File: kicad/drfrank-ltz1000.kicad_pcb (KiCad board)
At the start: 2 copper layers, 79.9 x 49.9 mm, 58 parts, among them IC1 LT1013, IC2 LTZ1000A, IC3 MAX420, J10 LINK, J11 LINK, Q1 BC639

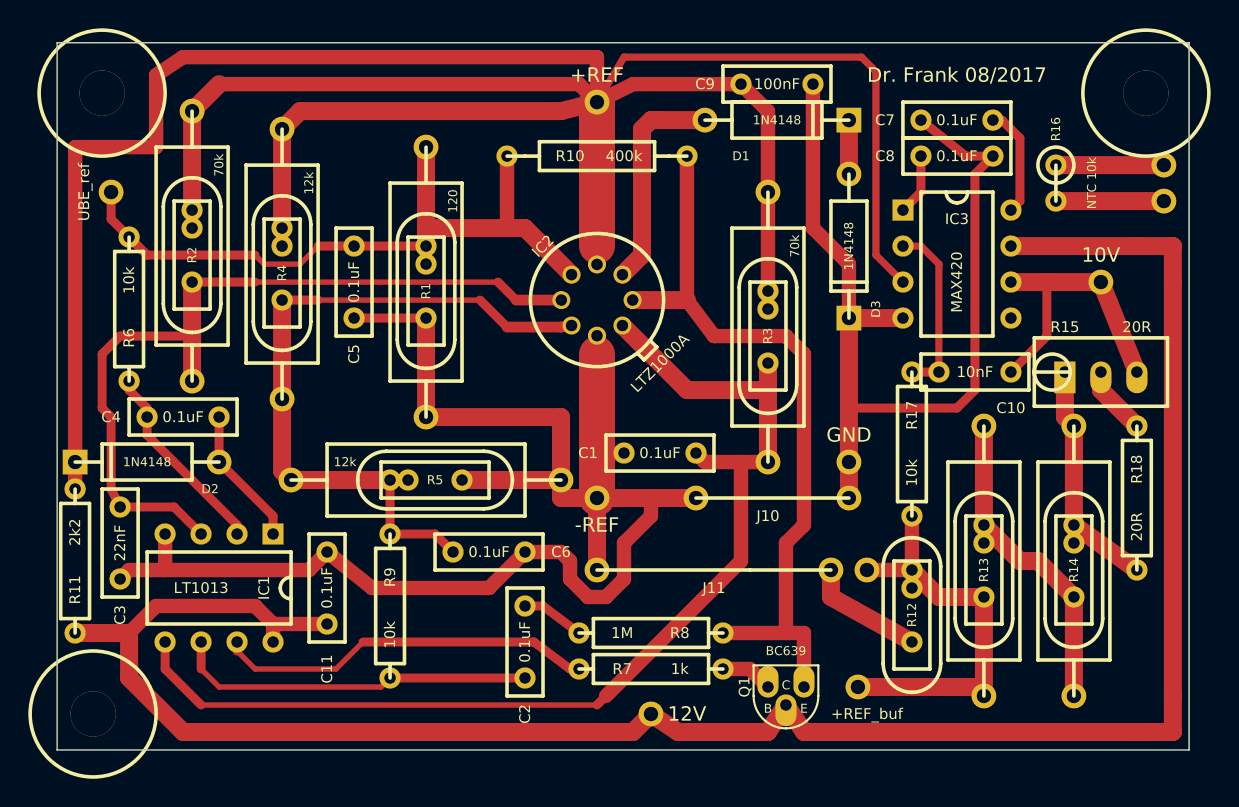
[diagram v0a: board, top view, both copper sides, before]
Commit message: moving copper to back side, adding copper links
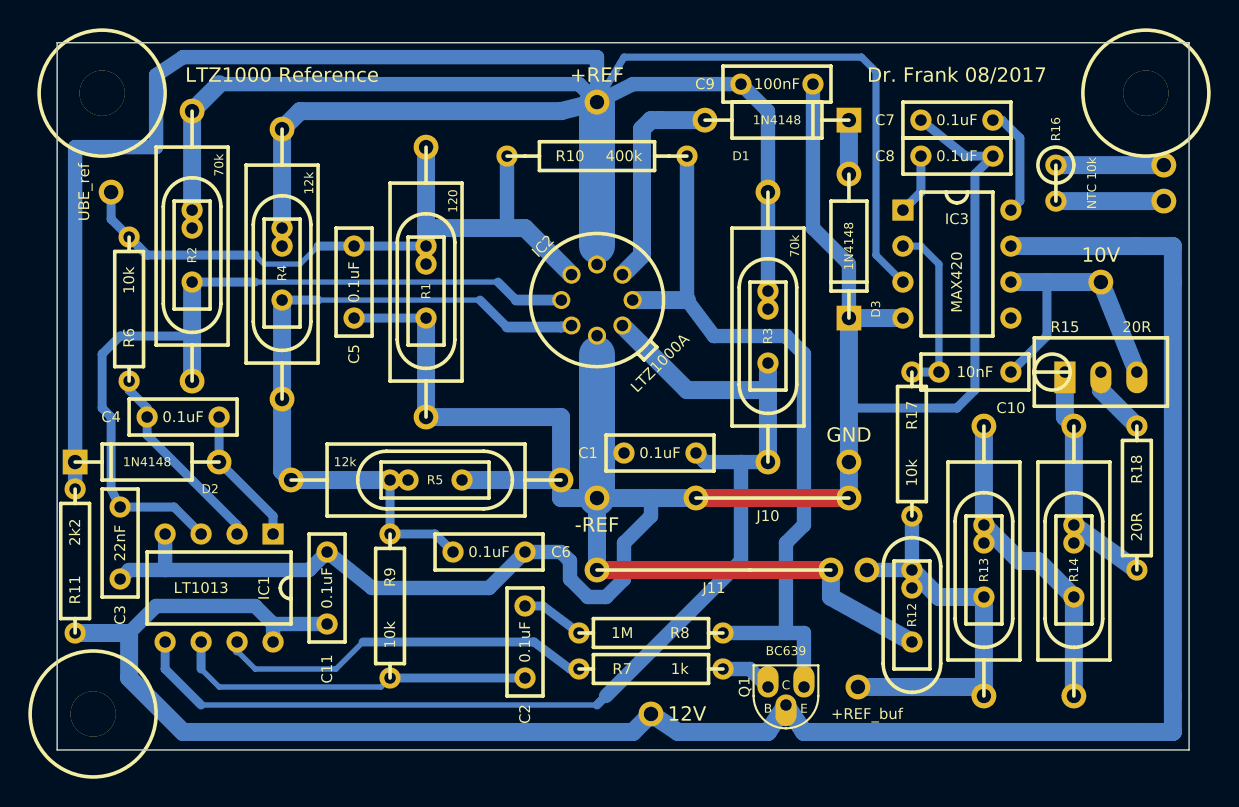
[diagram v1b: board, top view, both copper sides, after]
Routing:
- net -REF: track 187.1 -> 214.4 mm
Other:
- board text added: "LTZ1000 Reference"

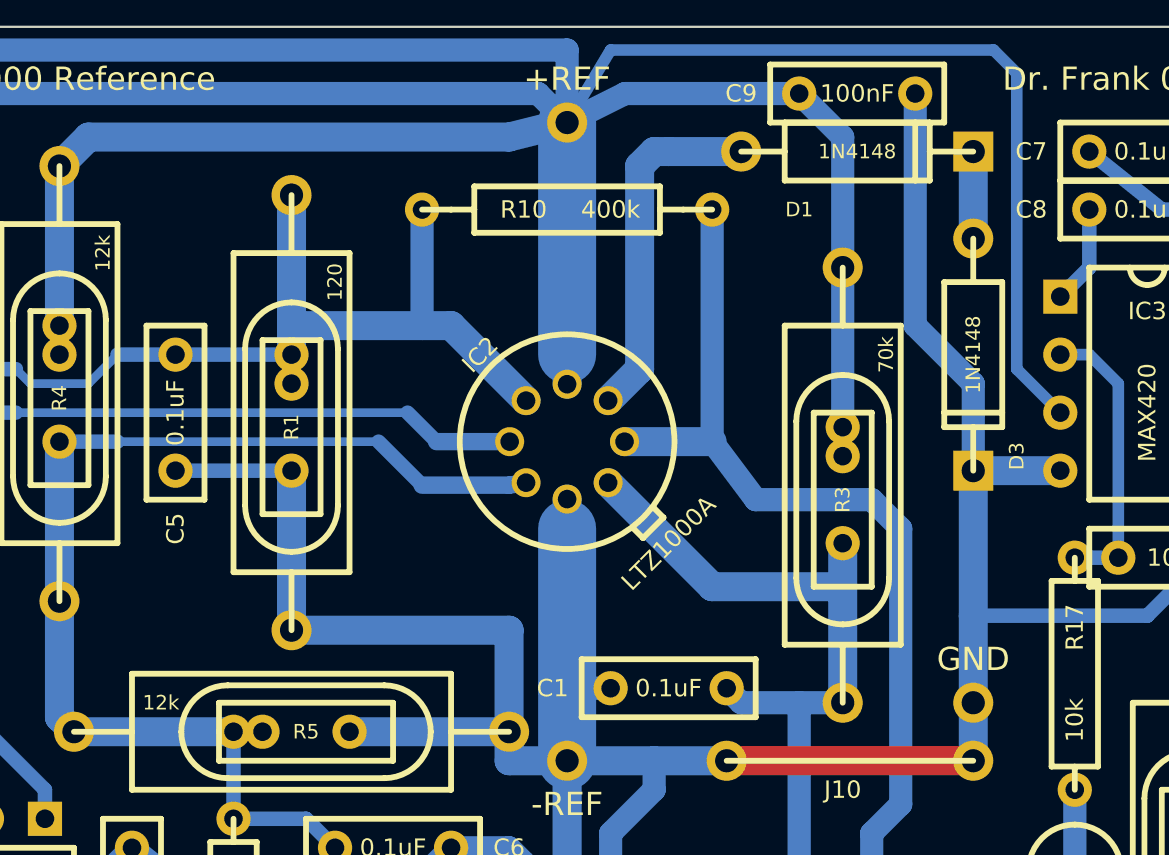
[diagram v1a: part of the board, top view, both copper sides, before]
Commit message: Omit D3.  Correct R5 label.
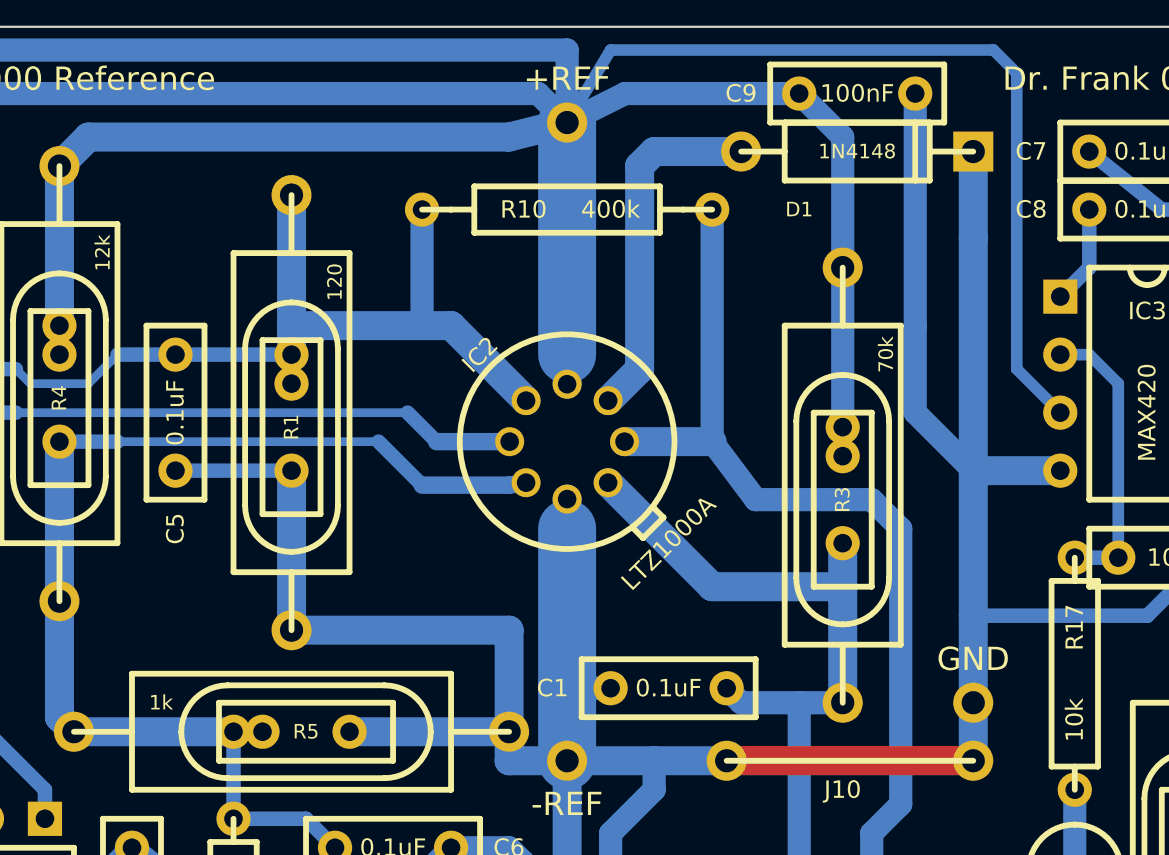
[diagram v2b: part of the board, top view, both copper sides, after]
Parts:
- removed D3: 1N4148, DIODE_1A_069A_PL
- R5: value 12k -> 1k
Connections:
- D1 pad 2: N-000007 (its old number) -> -REF
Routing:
- net -REF: track 214.4 -> 228.4 mm
- net N-000007 (its old number): track 3.81 -> 0.00 mm

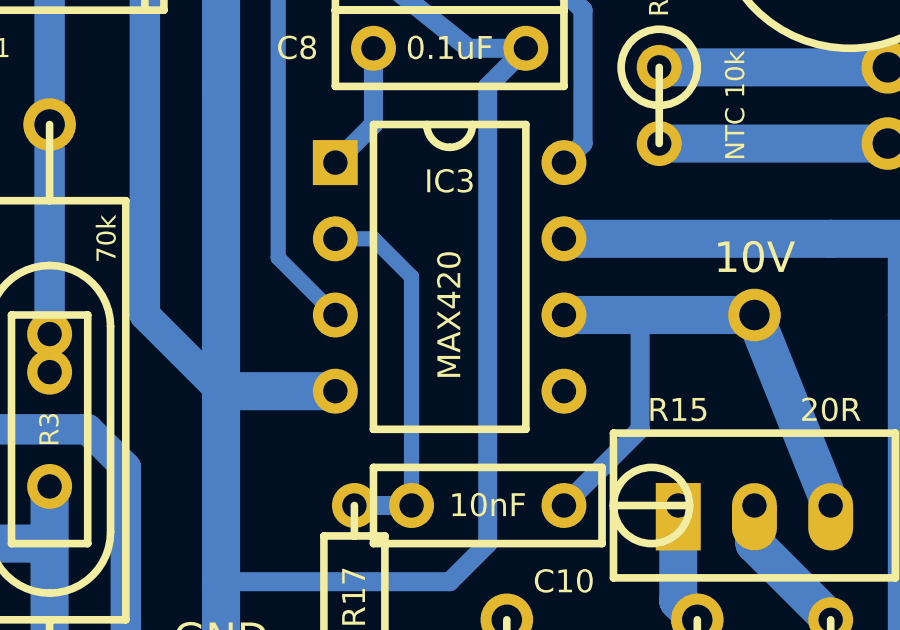
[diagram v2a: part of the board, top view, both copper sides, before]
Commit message: MAX420 -> LTC1052
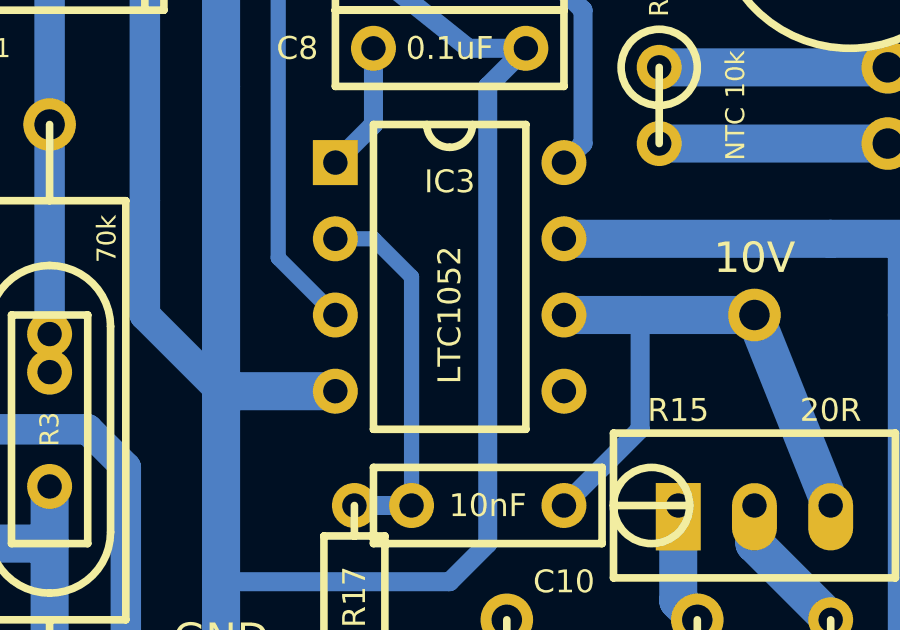
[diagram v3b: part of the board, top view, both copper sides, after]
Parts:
- IC3: value MAX420 -> LTC1052
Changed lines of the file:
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@@
   )
   (setup
-    (last_trace_width 1.016)
+    (last_trace_width 0.254)
     (user_trace_width 0.381)
     (user_trace_width 0.508)
@@
       (effects (font (size 0.762 0.762) (thickness 0.1524)))
     )
-    (fp_text value MAX420 (at 5.08 -3.81 270) (layer F.SilkS)
-      (effects (font (size 0.762 0.762) (thickness 0.1524)))
-    )
+    (fp_text value LTC1052 (at 5.08 -3.81 270) (layer F.SilkS)
+      (effects (font (size 0.762 0.762) (thickness 0.1524)))
+    )
